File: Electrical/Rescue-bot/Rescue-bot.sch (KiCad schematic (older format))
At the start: 20 parts

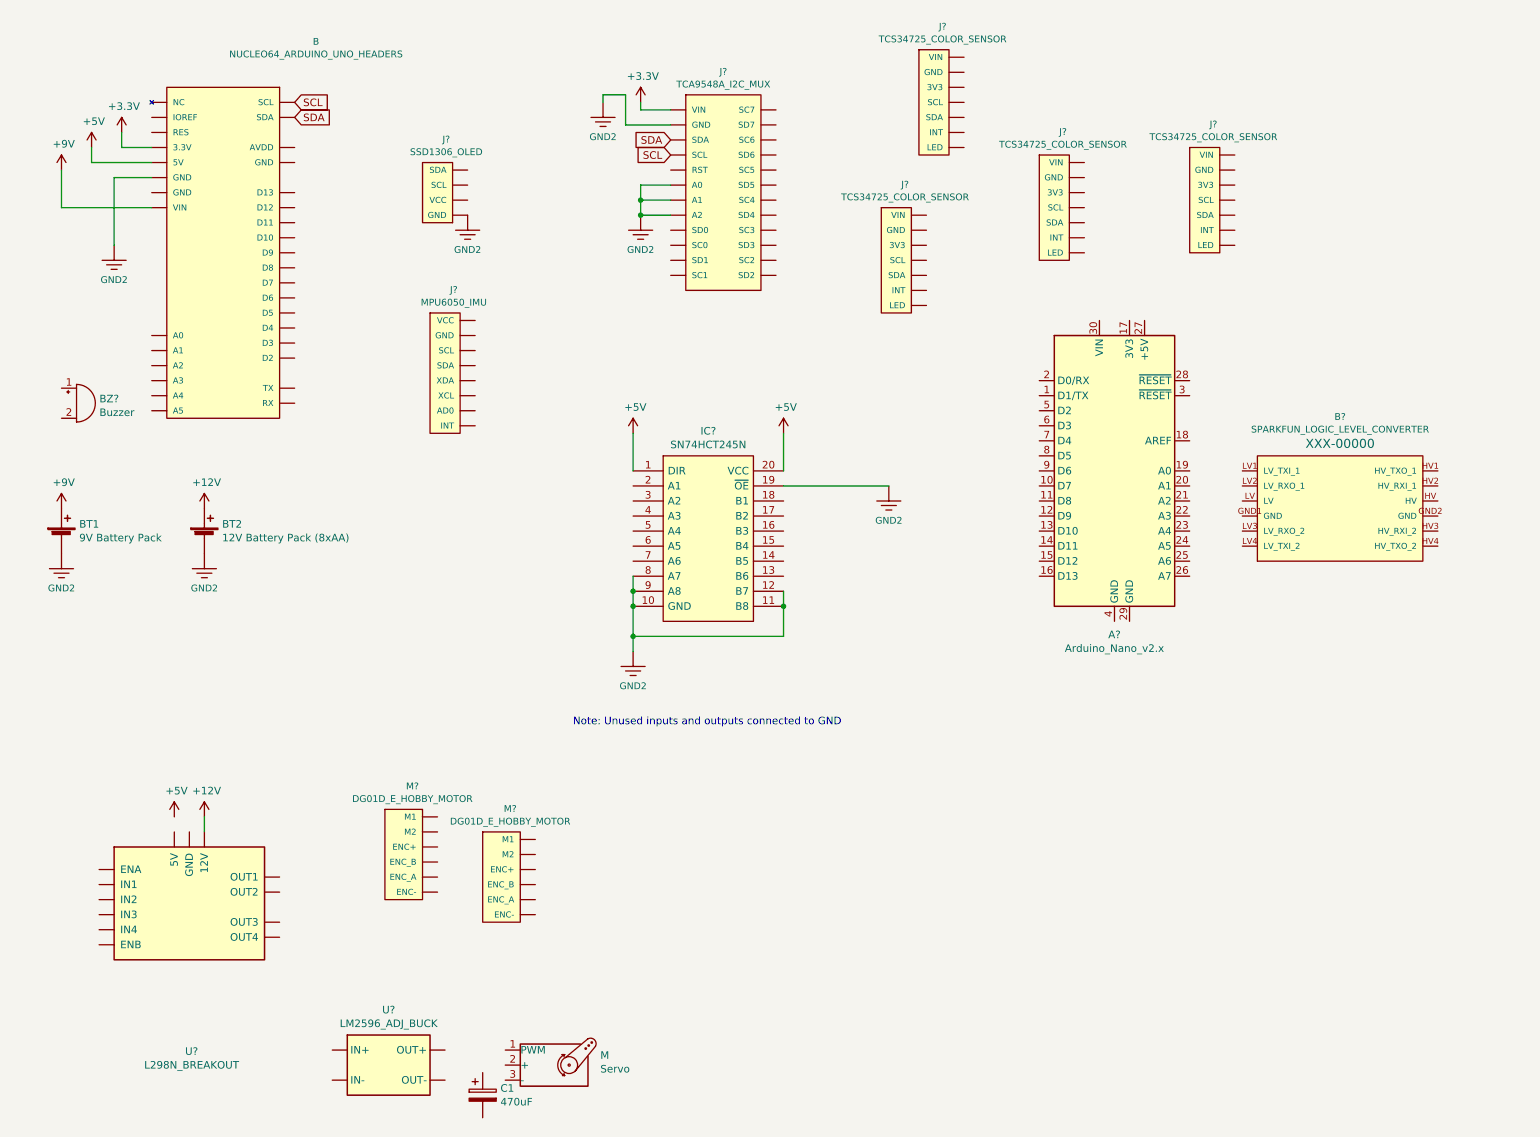
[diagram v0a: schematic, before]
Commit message: Schematic - Complete ColorSensors and Servo
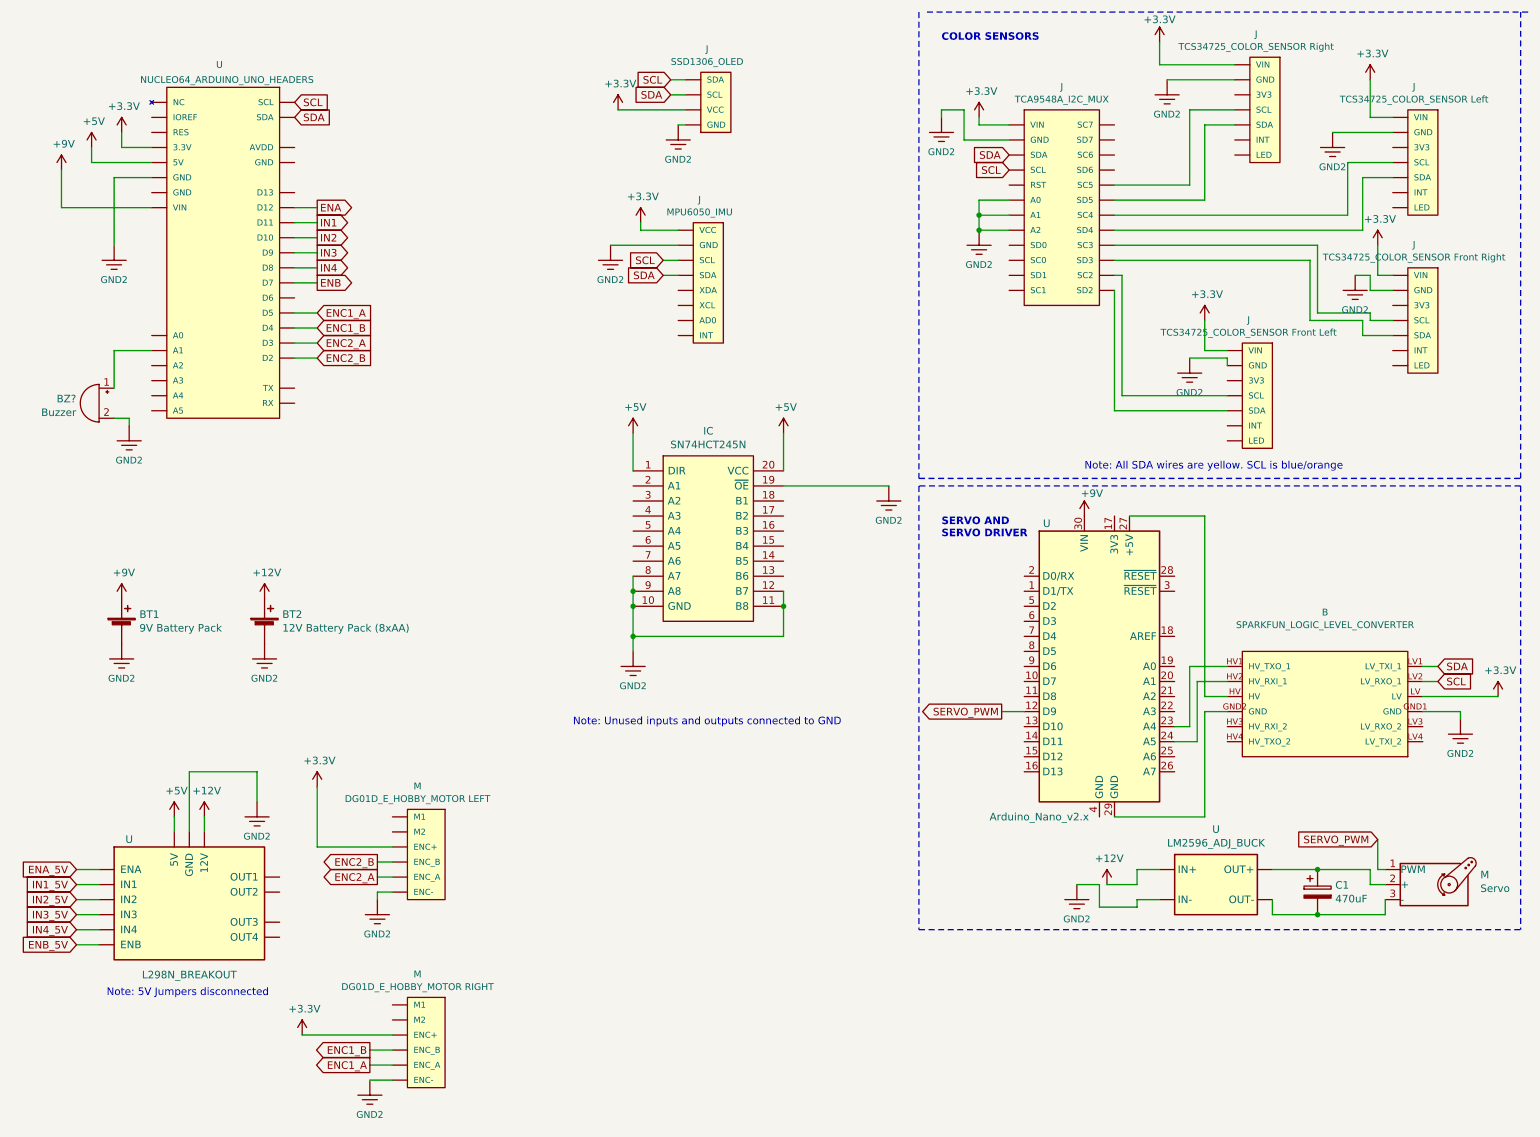
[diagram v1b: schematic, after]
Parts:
- B: renamed from B?; Field4 XXX-00000 -> (none)
- J: renamed from J?; value TCS34725_COLOR_SENSOR -> TCS34725_COLOR_SENSOR Front Right
- J: renamed from J?; value TCS34725_COLOR_SENSOR -> TCS34725_COLOR_SENSOR Left
- J: renamed from J?; value TCS34725_COLOR_SENSOR -> TCS34725_COLOR_SENSOR Right
- J: renamed from J?; value TCS34725_COLOR_SENSOR -> TCS34725_COLOR_SENSOR Front Left
- M: renamed from M?; value DG01D_E_HOBBY_MOTOR -> DG01D_E_HOBBY_MOTOR LEFT
- M: renamed from M?; value DG01D_E_HOBBY_MOTOR -> DG01D_E_HOBBY_MOTOR RIGHT
- gave numbers to parts that had none: 4
- renumbered B to U
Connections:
- net +12V: now also U.1 (IN+)
- net +3V3: now also B.LV, J.2 (VCC), J.7 (VCC), J.7 (VIN), J.7 (VIN), J.7 (VIN), J.7 (VIN), M.5 (ENC+), M.5 (ENC+)
- net +5V: now also U.9 (5V)
- net +9V: now also U.30 (VIN)
- net 3.3V: now also B.GND1 (GND), BZ?.2 (+), J.6 (GND), J.6 (GND), J.6 (GND), J.6 (GND), J.6 (GND), M.2 (ENC-), M.2 (ENC-), U.2 (IN-), U.8 (GND)
- net SCL: now also B.LV2 (LV_RXO_1), J.4 (SCL), J.4 (SDA)
- net SDA: now also B.LV1 (LV_TXI_1), J.3 (SCL), J.3 (SDA)
- net at U.A1: now also BZ?.1 (-)
- net IN2: now reaches U.D10
- net IN1: now reaches U.D11
- net ENA: now reaches U.D12
- net ENC2_B: now reaches U.D2
- net ENC2_B: now also M.4 (ENC_B)
- net ENC2_A: now reaches U.D3
- net ENC2_A: now also M.3 (ENC_A)
- net ENC1_B: now reaches U.D4
- net ENC1_B: now also M.4 (ENC_B)
- net ENC1_A: now reaches U.D5
- net ENC1_A: now also M.3 (ENC_A)
- net ENB: now reaches U.D7
- net IN4: now reaches U.D8
- net IN3: now reaches U.D9
- net at J.3 (SDA): now also J.15 (SD3)
- net at J.4 (SCL): now also J.16 (SC3)
- net IN3_5V: now reaches U.10 (IN3)
- net ENB_5V: now reaches U.11 (ENB)
- net IN4_5V: now reaches U.12 (IN4)
- net IN1_5V: now reaches U.5 (IN1)
- net ENA_5V: now reaches U.6 (ENA)
- net IN2_5V: now reaches U.7 (IN2)
- net at C1.1: now also M.2 (+), U.4 (OUT+)
- net at C1.2: now also M.3 (-), U.3 (OUT-)
- net SERVO_PWM: now reaches M.1 (PWM)
- net SERVO_PWM: now also U.12 (D9)
- net at U.23 (A4): now also B.HV1 (HV_TXO_1)
- net at U.24 (A5): now also B.HV2 (HV_RXI_1)
- net at U.27 (+5V): now also B.HV
- net at U.29 (GND): now also B.GND2 (GND)
- net at J.13 (SD2): now also J.3 (SDA)
- net at J.14 (SC2): now also J.4 (SCL)
- net at J.17 (SD4): now also J.3 (SDA)
- net at J.18 (SC4): now also J.4 (SCL)
- net at J.19 (SD5): now also J.3 (SDA)
- net at J.20 (SC5): now also J.4 (SCL)
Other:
- note added: "COLOR SENSORS"
- note added: "Note: 5V Jumpers disconnected"
- note added: "Note: All SDA wires are yellow. SCL is blue/orange"
- note added: "SERVO AND \nSERVO DRIVER"
- moved on the sheet: B, BT1, BT2, BZ?, C1, J, M, U

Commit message: Finish Schematic
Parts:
- gave numbers to parts that had none: 1
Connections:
- net 3.3V: now also J.1 (INT)
- net ENA: now also IC.7 (A6)
- net ENA_5V: now also IC.13 (B6)
- net ENB: now also IC.2 (A1)
- net ENB_5V: now also IC.18 (B1)
- net IN1: now also IC.6 (A5)
- net IN1_5V: now also IC.14 (B5)
- net IN2: now also IC.5 (A4)
- net IN2_5V: now also IC.15 (B4)
- net IN3: now also IC.4 (A3)
- net IN3_5V: now also IC.16 (B3)
- net IN4: now also IC.3 (A2)
- net IN4_5V: now also IC.17 (B2)
- net at U.13 (OUT3): now also M.7 (M1)
- net at U.14 (OUT4): now also M.6 (M2)
- net at U.2 (OUT1): now also M.7 (M1)
- net at U.3 (OUT2): now also M.6 (M2)
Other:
- note added: "128x64 Monochrome OLED"
- note added: "BATTERIES"
- note added: "Blue Wire"
- note added: "Green Wire"
- note added: "MOTORS, MOTOR DRIVER, AND LEVEL SHIFTING"
- note added: "NUCLEO64, IMU, OLED"
- note added: "Nucleo-F401RE"
- note added: "RESCUE-BOT"
- moved on the sheet: BT1, BT2, BZ, IC, J, M, U
